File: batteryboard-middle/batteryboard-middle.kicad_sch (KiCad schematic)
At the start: 8 parts, among them J2 Conn_01x02, J3 Conn_01x02

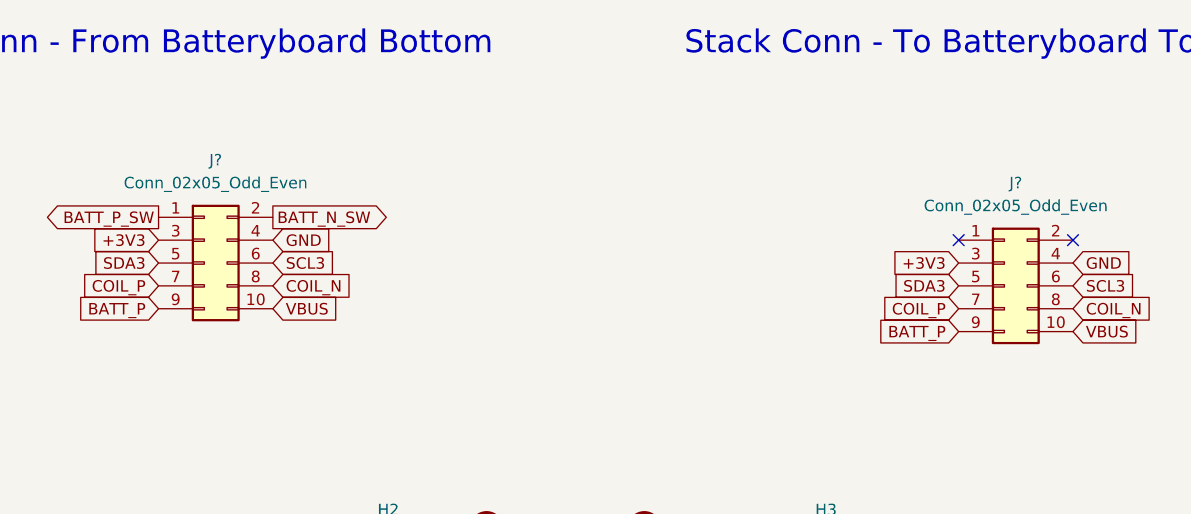
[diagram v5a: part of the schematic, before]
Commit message: Added proper connectors and added traces
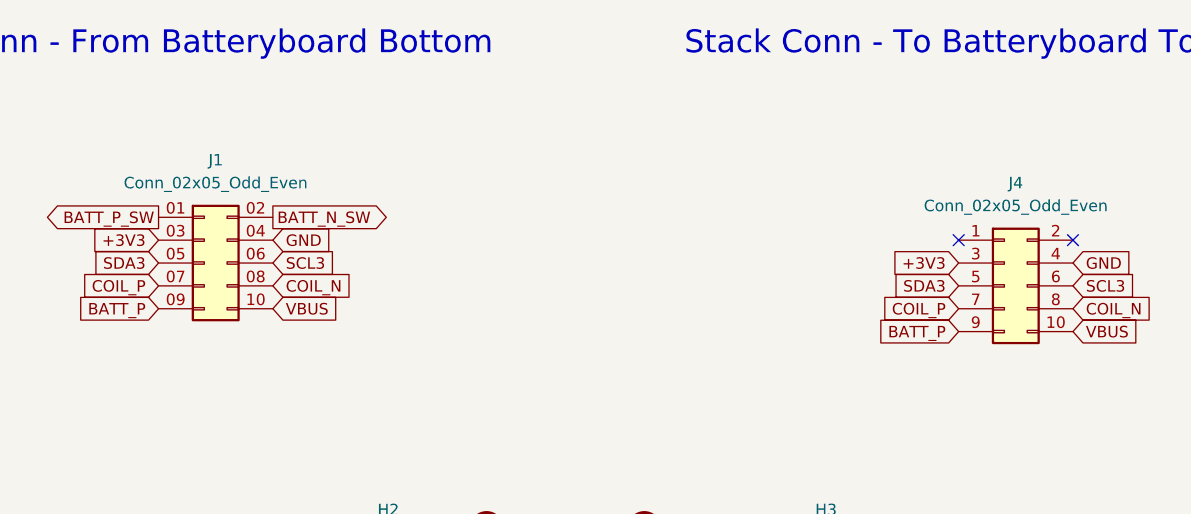
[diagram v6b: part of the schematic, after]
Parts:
- J1: renamed from J?; footprint (none) -> batteryboard:SAMTEC_FLE-105-01-G-DV-A
- J4: renamed from J?; footprint (none) -> batteryboard:SAMTEC-FTS-105-01-X-DV
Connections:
- net +3V3: now also J1.03 (Pin_3); no longer J1.3 (Pin_3)
- net BATT_N_SW: now also J1.02 (Pin_2); no longer J1.2 (Pin_2)
- net BATT_P: now also J1.09 (Pin_9); no longer J1.9 (Pin_9)
- net BATT_P_SW: now also J1.01 (Pin_1); no longer J1.1 (Pin_1)
- net COIL_N: now also J1.08 (Pin_8); no longer J1.8 (Pin_8)
- net COIL_P: now also J1.07 (Pin_7); no longer J1.7 (Pin_7)
- net GND: now also J1.04 (Pin_4); no longer J1.4 (Pin_4)
- net SCL3: now also J1.06 (Pin_6); no longer J1.6 (Pin_6)
- net SDA3: now also J1.05 (Pin_5); no longer J1.5 (Pin_5)
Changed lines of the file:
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@@
     (pin "1")
   )
-  (symbol (lib_id "Connector_Generic:Conn_02x05_Odd_Even") (at 63.5 53.34 0) (unit 1)
+  (symbol (lib_name "Conn_02x05_Odd_Even_1") (lib_id "Connector_Generic:Conn_02x05_Odd_Even") (at 63.5 53.34 0) (unit 1)
     (in_bom yes) (on_board yes) (fields_autoplaced)
-    (property "Reference" "J?" (id 0) (at 64.77 41.91 0))
+    (property "Reference" "J1" (id 0) (at 64.77 41.91 0))
     (property "Value" "Conn_02x05_Odd_Even" (id 1) (at 64.77 44.45 0))
-    (property "Footprint" "" (id 2) (at 63.5 53.34 0)
+    (property "Footprint" "batteryboard:SAMTEC_FLE-105-01-G-DV-A" (id 2) (at 63.5 45.72 0)
       (effects (font (size 1.27 1.27)) hide)
     )
@@
       (effects (font (size 1.27 1.27)) hide)
     )
-    (pin "1")
+    (pin "01")
     (pin "10")
-    (pin "2")
-    (pin "3")
-    (pin "4")
-    (pin "5")
-    (pin "6")
-    (pin "7")
-    (pin "8")
-    (pin "9")
+    (pin "02")
+    (pin "03")
+    (pin "04")
+    (pin "05")
+    (pin "06")
+    (pin "07")
+    (pin "08")
+    (pin "09")
   )
   (symbol (lib_id "Mechanical:MountingHole_Pad") (at 113.665 88.265 90) (unit 1)
@@
   (symbol (lib_id "Connector_Generic:Conn_02x05_Odd_Even") (at 152.4 55.88 0) (unit 1)
     (in_bom yes) (on_board yes) (fields_autoplaced)
-    (property "Reference" "J?" (id 0) (at 153.67 44.45 0))
+    (property "Reference" "J4" (id 0) (at 153.67 44.45 0))
     (property "Value" "Conn_02x05_Odd_Even" (id 1) (at 153.67 46.99 0))
-    (property "Footprint" "" (id 2) (at 152.4 55.88 0)
+    (property "Footprint" "batteryboard:SAMTEC-FTS-105-01-X-DV" (id 2) (at 152.4 55.88 0)
       (effects (font (size 1.27 1.27)) hide)
     )
@@
       (reference "H4") (unit 1) (value "MountingHole_Pad") (footprint "mainboard:MountingHole")
     )
+    (path "/8797612e-14ed-44eb-a090-2a8aad427753"
+      (reference "J1") (unit 1) (value "Conn_02x05_Odd_Even") (footprint "batteryboard:SAMTEC_FLE-105-01-G-DV-A")
+    )
     (path "/ec4bc908-aaa7-48e1-8392-751477465b2b"
       (reference "J2") (unit 1) (value "Conn_01x02") (footprint "batteryboard:Battery Pads")
@@
       (reference "J3") (unit 1) (value "Conn_01x02") (footprint "batteryboard:Battery Pads")
     )
-    (path "/8797612e-14ed-44eb-a090-2a8aad427753"
-      (reference "J?") (unit 1) (value "Conn_02x05_Odd_Even") (footprint "")
-    )
     (path "/df586b02-02b3-429d-a0c0-fe4a87110a37"
-      (reference "J?") (unit 1) (value "Conn_02x05_Odd_Even") (footprint "")
+      (reference "J4") (unit 1) (value "Conn_02x05_Odd_Even") (footprint "batteryboard:SAMTEC-FTS-105-01-X-DV")
     )
   )

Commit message: Fixes and cleanup
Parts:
- J4: footprint batteryboard:SAMTEC-FTS-105-01-X-DV -> batteryboard:FTS-105-XX-YY-DV-A
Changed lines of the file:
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@@
     )
     (pin "01")
-    (pin "10")
     (pin "02")
     (pin "03")
@@
     (pin "08")
     (pin "09")
+    (pin "10")
   )
   (symbol (lib_id "Mechanical:MountingHole_Pad") (at 113.665 88.265 90) (unit 1)
@@
     (property "Reference" "J4" (id 0) (at 153.67 44.45 0))
     (property "Value" "Conn_02x05_Odd_Even" (id 1) (at 153.67 46.99 0))
-    (property "Footprint" "batteryboard:SAMTEC-FTS-105-01-X-DV" (id 2) (at 152.4 55.88 0)
+    (property "Footprint" "batteryboard:FTS-105-XX-YY-DV-A" (id 2) (at 152.4 55.88 0)
       (effects (font (size 1.27 1.27)) hide)
     )
@@
     )
     (path "/df586b02-02b3-429d-a0c0-fe4a87110a37"
-      (reference "J4") (unit 1) (value "Conn_02x05_Odd_Even") (footprint "batteryboard:SAMTEC-FTS-105-01-X-DV")
+      (reference "J4") (unit 1) (value "Conn_02x05_Odd_Even") (footprint "batteryboard:FTS-105-XX-YY-DV-A")
     )
   )
